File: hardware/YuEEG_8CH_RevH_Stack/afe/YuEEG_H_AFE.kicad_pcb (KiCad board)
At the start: 4 copper layers, 48 x 60 mm, 138 parts, among them J1301 1x10 2.54mm RIGHT ANGLE / ELE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, U1 ADS1299PAG, U401 TPS7A4901DGNR, U403 TPS73225DBVR, U404 TPS60403DBVR, U405 TPS72325DBVR

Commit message: Refine Rev H module legends and USB return paths
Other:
- board text added: "ADS1299"
- board text added: "POWER"

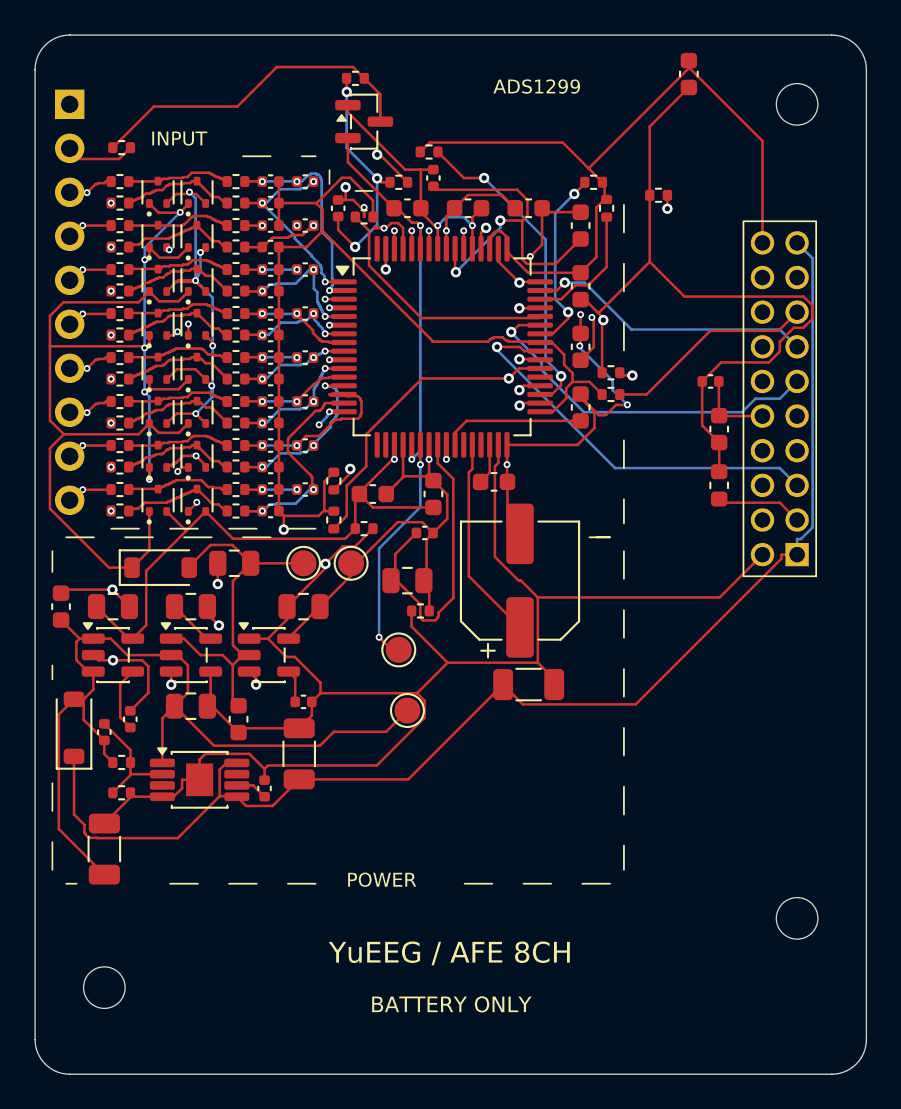
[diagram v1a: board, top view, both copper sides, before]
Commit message: Refine stacked AFE clearance and rounded USB mouth geometry
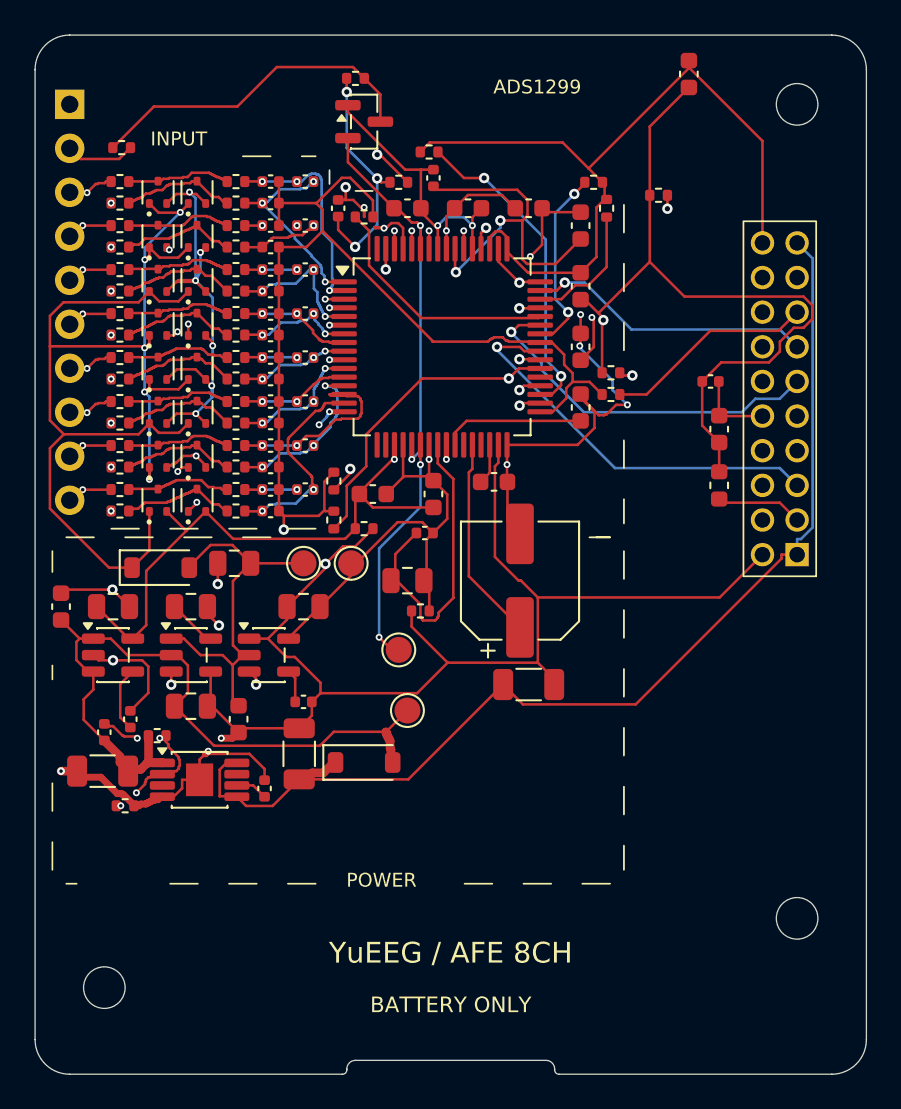
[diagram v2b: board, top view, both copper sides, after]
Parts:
- C405: value 22u 16V X7R -> 22u 16V X7R MSASE31LBB7226MTNA01; footprint Capacitor_SMD:C_1206_3216Metric -> YuEEG:TY_MSASE31LBB7226MTNA01_1206
- moved D403 16.9 mm to (19.0, 42.0), turned to 0 degrees
- moved C405 4.50 mm to (3.90, 42.5), turned to 180 degrees
- moved R401 2.57 mm to (7.05, 40.5)
- moved R402 0.78 mm to (5.20, 44.5)
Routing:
- net SYS_5V: track 75.9 -> 64.7 mm
- net +4V4_PRE: track 50.8 -> 41.5 mm
- net GND: track 258.1 -> 251.3 mm, vias 5 -> 8
- net LDO_FB: track 6.87 -> 10.6 mm, vias 0 -> 4
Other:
- outline, holes or cut-outs redrawn
